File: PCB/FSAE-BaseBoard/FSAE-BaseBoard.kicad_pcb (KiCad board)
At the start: 2 copper layers, 100 x 100 mm, 71 parts, among them J1 Conn_01x14_Socket, J10 Conn_01x03, J11 Zocalo_Resolver, J12 Bornera_Resolver, J13 Zocalo_Resolver, J14 Screw_Terminal_01x03, J15 Bornera_Encoder, J3 Conn_01x03, J4 Conn_01x02, J5 Conn_01x02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

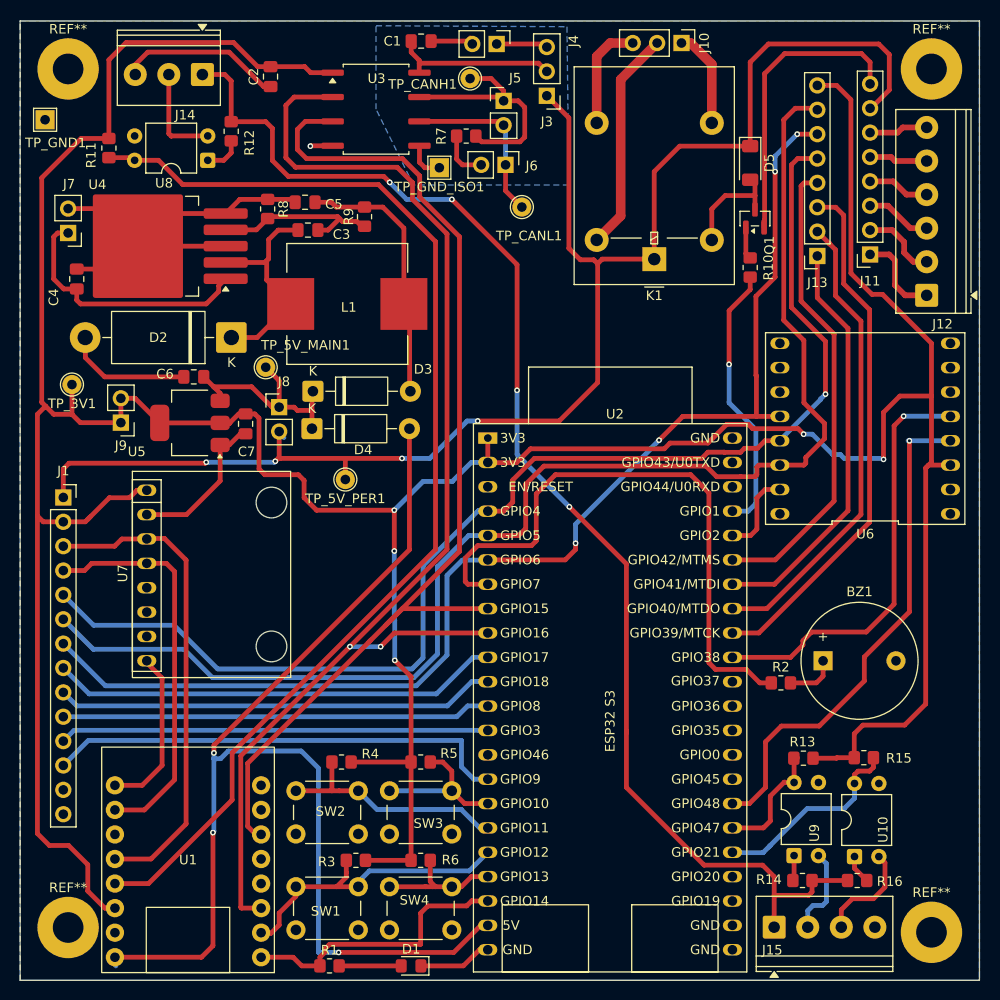
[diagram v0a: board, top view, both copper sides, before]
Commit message: Reduccion de vias
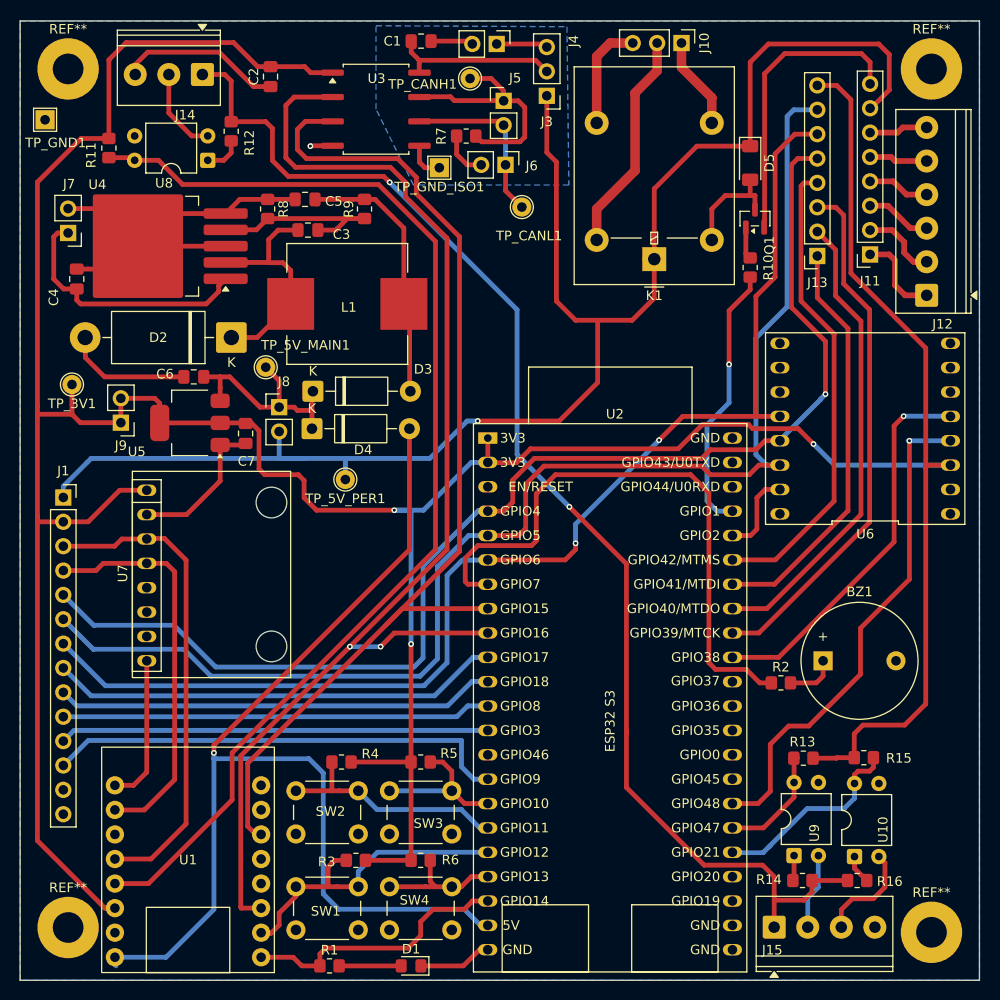
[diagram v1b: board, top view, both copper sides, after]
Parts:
- moved C7 1.00 mm to (74.0, 94.0)
- moved R9 0.80 mm to (86.4, 70.6)
- moved C5 0.30 mm to (80.2, 69.6)
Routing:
- net /Bloque de Alimentacion/V_USB: track 123.2 -> 114.9 mm, vias 3 -> 1
- net +5V: track 158.4 -> 165.5 mm, vias 4 -> 1
- net +3.3V: track 397.6 -> 392.6 mm, vias 5 -> 3
- net /ESP32 C3 y S3/INT_LORA: track 44.3 -> 40.2 mm
- net +12V: track 138.4 -> 135.9 mm, vias 4 -> 2
- net /ESP32 C3 y S3/MOSI: track 141.0 -> 138.5 mm
- net Net-(U4-FB): track 18.2 -> 20.3 mm
- net /ESP32 C3 y S3/INT_MPU: track 17.3 -> 15.5 mm
- net /ESP32 C3 y S3/BTN_1: track 31.9 -> 33.6 mm
- net /Perifericos/ENC_A_RAW: track 9.20 -> 7.92 mm
- net /Perifericos/Señal_12V: track 10.3 -> 9.06 mm
- net GND: track 130.9 -> 129.7 mm
- net /ESP32 C3 y S3/LED_ESTADO: track 29.5 -> 28.4 mm
- net Net-(D2-K): track 23.3 -> 24.1 mm
- net Net-(D3-K): track 23.2 -> 23.9 mm
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
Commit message: ModificacionesByNico
Corregi una eleccion de footprint y arregle un poco el layout tambien detecte una falla que no solucione que es el echo que los smd y lo th van a tener problemas para soldarlos
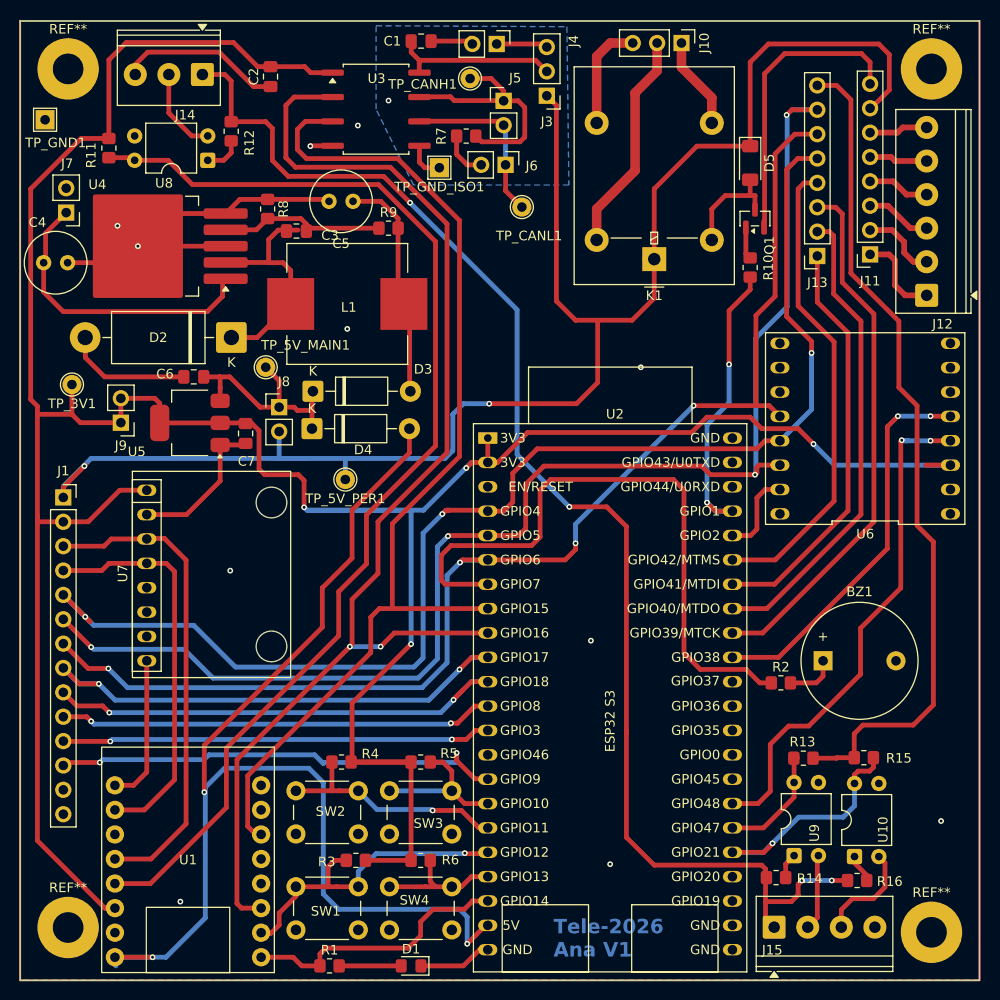
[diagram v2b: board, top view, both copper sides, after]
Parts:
- C4, C5: footprint Capacitor_SMD:C_0805_2012Metric_Pad1.18x1.45mm_HandSolder -> Capacitor_THT:C_Radial_D6.3mm_H11.0mm_P2.50mm
- moved C5 5.00 mm to (85.2, 69.8)
- moved C4 3.85 mm to (53.0, 76.2), turned to 0 degrees
- moved R9 3.20 mm to (88.9, 72.6), turned to 0 degrees
- moved R14 2.77 mm to (129.3, 140.3), turned to 0 degrees
- moved J7 2.13 mm to (55.3, 71.0)
- moved C3 1.20 mm to (79.3, 72.9)
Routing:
- net +3.3V: track 392.6 -> 415.8 mm, vias 3 -> 4
- net /Bloque de Alimentacion/V_USB: track 114.9 -> 127.8 mm, vias 1 -> 3
- net +5V: track 165.5 -> 172.1 mm, vias 1 -> 2
- net /ESP32 C3 y S3/MISO: track 130.3 -> 136.6 mm, vias 1 -> 3
- net /ESP32 C3 y S3/UART1_TX: track 47.1 -> 53.4 mm, vias 0 -> 2
- net +12V: track 135.9 -> 142.0 mm, vias 2 -> 4
- net /ESP32 C3 y S3/ENC_B: track 21.1 -> 26.2 mm, vias 0 -> 1
- net +5VA: track 28.1 -> 23.7 mm
- net /Bloque de Alimentacion/VIN_BAT: track 27.2 -> 31.5 mm
- net /ESP32 C3 y S3/CTRL_BUZZER: track 62.6 -> 66.9 mm
- net GND: track 129.7 -> 133.9 mm, vias 1 -> 11
- net /ESP32 C3 y S3/UART1_RX: track 45.9 -> 49.5 mm, vias 0 -> 2
- net /ESP32 C3 y S3/SCK: track 128.8 -> 132.0 mm, vias 2 -> 4
- net /ESP32 C3 y S3/MOSI: track 138.5 -> 141.7 mm, vias 0 -> 4
- net /ESP32 C3 y S3/CTRL_RELE: track 28.3 -> 31.4 mm, vias 1 -> 2
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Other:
- board text added: "Tele-2026 Ana V1"
